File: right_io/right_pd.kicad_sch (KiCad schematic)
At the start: 68 parts, among them J11 USB-C dual-role data/PD port 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, J12 USB-C source-only data port J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, Q2002 2N7002K DFP USB2 enable inver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, U1760 TPS2553DDBVR 1.3A USB branch, U1761 TPS25810RVCR Type-C DFP contr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, U1763 TPD1S514-1YZR 5.9V VBUS OVP, U1765 TPD4E05U06 USB2/CC ESD, U2011 TPD4S201 CC and USB2 short-to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, U2012 CAT24C256 32KB private TPS257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, U2013 TS3USB30E DFP-qualified USB2 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, U2014 SN74LVC2G07 partial-power-dow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, U2015 TVS2200 22V USB VBUS surge cl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, U2016 SN74LVC1G08 DFP and attached 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, U42 TPS25751AD USB-PD DRP control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, U721 TPS26630RGER PD2 default-off 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

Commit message: Phase 5: second-opinion audit remediation + rebuilt, verified board pipeline
Second-opinion AI audit found A-tier defects; remediation applied and the
board pipeline rebuilt on a known-good base with the fixes it needed:

- electrical: LTC4418IUF symbol pinout corrected (both selectors were
  dead as drawn); center charge cascade (U15 <- U15B, PD1 > PD2 > AUX);
  pack negative never crosses FPC-3, 15-pin FG_VSS return; power-budgeted
  FPC pin maps (0.4 A/pin derate); J12/DS4 completed; AUX source fuse
- FH41-68S footprint: 13 datasheet-correct SH pads + SH pin in symbol
- connector geometry settled against the Hirose FH12 2D drawing: FFC
  enters opposite the solder pins (mouth = local +Y); reversed side-B
  maps are correct for the 180-deg-mounted pairs; rotations set so mouths
  face across every seam
- pipeline (generate_split_boards.py): per-pin pad-net resync from the
  netlists (kills shadow nets for good), netlist-exact name
  normalization, netlist-only part injection (cascade, probe headers),
  zone refill after outline swap, read-before-write race fixed, orphan
  parts dropped loudly, non-zero exit on unresolved overlaps
- monolith board relocated to old/monolith_ducktop2.kicad_pcb (placement
  oracle for the center cut only)

verified end state: 4 boards 0 shorts / 0 clearance / 0 drill, 0 boundary
crossings, 6/6 connectors contract-exact with mouths facing, 0 shadow
nets, gates PASS x4, ERC 0 x4. routing next (499 nets/board).
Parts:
- added H13, H15, H17, H27: M2.5 isolated mainboard mounting hole, MountingHole:MountingHole_2.7mm_M2.5, symbol Mechanical:MountingHole
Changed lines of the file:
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@@
 )
 (no_connect (at 388.62 147.32))
-(label "PD2_VBUS_GATED"
+(hierarchical_label "PD2_VBUS_GATED"
+  (shape bidirectional)
   (at 388.62 132.08 0)
   (effects (font (size 1.27 1.27)) (justify left bottom))
 )
-(label "PD2_VBUS_GATED"
+(hierarchical_label "PD2_VBUS_GATED"
+  (shape bidirectional)
   (at 388.62 132.08 0)
   (effects (font (size 1.27 1.27)) (justify left bottom))
@@
   (effects (font (size 1.27 1.27)) (justify left bottom))
 )
-(label "HUB_PRT_CTL4"
+(hierarchical_label "HUB_PRT_CTL4"
+  (shape bidirectional)
   (at 38.1 359.41 0)
   (effects (font (size 1.27 1.27)) (justify left bottom))
 )
-(label "HUB_PRT_CTL4"
+(hierarchical_label "HUB_PRT_CTL4"
+  (shape bidirectional)
   (at 53.34 361.95 0)
   (effects (font (size 1.27 1.27)) (justify left bottom))
@@
   )
 )
-(label "HUB_PRT_CTL4"
+(hierarchical_label "HUB_PRT_CTL4"
+  (shape bidirectional)
   (at 111.76 381 0)
   (effects (font (size 1.27 1.27)) (justify left bottom))
@@
   (effects (font (size 1.27 1.27)) (justify left bottom))
 )
-(label "HUB_PRT_CTL4"
+(hierarchical_label "HUB_PRT_CTL4"
+  (shape bidirectional)
   (at 86.36 375.92 0)
   (effects (font (size 1.27 1.27)) (justify left bottom))
@@
   (effects (font (size 1.27 1.27)) (justify left bottom))
 )
-(label "HUB_DS4_DP"
+(hierarchical_label "HUB_DS4_DP"
+  (shape bidirectional)
   (at 261.62 373.38 0)
   (effects (font (size 1.27 1.27)) (justify left bottom))
 )
-(label "HUB_DS4_DP"
+(hierarchical_label "HUB_DS4_DP"
+  (shape bidirectional)
   (at 261.62 375.92 0)
   (effects (font (size 1.27 1.27)) (justify left bottom))
 )
-(label "HUB_DS4_DM"
+(hierarchical_label "HUB_DS4_DM"
+  (shape bidirectional)
   (at 261.62 368.3 0)
   (effects (font (size 1.27 1.27)) (justify left bottom))
 )
-(label "HUB_DS4_DM"
+(hierarchical_label "HUB_DS4_DM"
+  (shape bidirectional)
   (at 261.62 370.84 0)
   (effects (font (size 1.27 1.27)) (justify left bottom))
@@
 (no_connect (at 271.78 398.78))
 (symbol
+  (lib_id "Mechanical:MountingHole")
+  (at 500.38 20.32 0)
+  (unit 1)
+  (exclude_from_sim no)
+  (in_bom no)
+  (on_board yes)
+  (dnp no)
+  (property "Reference" "H13" (at 500.38 17.78 0) (effects (font (size 1.27 1.27))))
+  (property "Value" "M2.5 isolated mainboard mounting hole" (at 500.38 22.86 0) (effects (font (size 1.27 1.27))))
+  (property "Footprint" "MountingHole:MountingHole_2.7mm_M2.5" (at 500.38 20.32 0) (effects (font (size 1.27 1.27)) (hide yes)))
+  (property "Datasheet" "" (at 500.38 20.32 0) (effects (font (size 1.27 1.27)) (hide yes)))
+  (property "Hardware_Spec" "2.7mm isolated NPTH for M2.5 chassis screw" (at 500.38 20.32 0) (effects (font (size 1.27 1.27)) (hide yes)))
+  (instances
+    (project "ducktop2"
+      (path "/37367af8-d35a-52ce-9a32-1764ce5de36b"
+        (reference "H13")
+        (unit 1)
+      )
+    )
+  )
+)
+(symbol
+  (lib_id "Mechanical:MountingHole")
+  (at 500.38 20.32 0)
+  (unit 1)
+  (exclude_from_sim no)
+  (in_bom no)
+  (on_board yes)
+  (dnp no)
+  (property "Reference" "H15" (at 500.38 17.78 0) (effects (font (size 1.27 1.27))))
+  (property "Value" "M2.5 isolated mainboard mounting hole" (at 500.38 22.86 0) (effects (font (size 1.27 1.27))))
+  (property "Footprint" "MountingHole:MountingHole_2.7mm_M2.5" (at 500.38 20.32 0) (effects (font (size 1.27 1.27)) (hide yes)))
+  (property "Datasheet" "" (at 500.38 20.32 0) (effects (font (size 1.27 1.27)) (hide yes)))
+  (property "Hardware_Spec" "2.7mm isolated NPTH for M2.5 chassis screw" (at 500.38 20.32 0) (effects (font (size 1.27 1.27)) (hide yes)))
+  (instances
+    (project "ducktop2"
+      (path "/37367af8-d35a-52ce-9a32-1764ce5de36b"
+        (reference "H15")
+        (unit 1)
+      )
+    )
+  )
+)
+(symbol
+  (lib_id "Mechanical:MountingHole")
+  (at 500.38 20.32 0)
+  (unit 1)
+  (exclude_from_sim no)
+  (in_bom no)
+  (on_board yes)
+  (dnp no)
+  (property "Reference" "H17" (at 500.38 17.78 0) (effects (font (size 1.27 1.27))))
+  (property "Value" "M2.5 isolated mainboard mounting hole" (at 500.38 22.86 0) (effects (font (size 1.27 1.27))))
+  (property "Footprint" "MountingHole:MountingHole_2.7mm_M2.5" (at 500.38 20.32 0) (effects (font (size 1.27 1.27)) (hide yes)))
+  (property "Datasheet" "" (at 500.38 20.32 0) (effects (font (size 1.27 1.27)) (hide yes)))
+  (property "Hardware_Spec" "2.7mm isolated NPTH for M2.5 chassis screw" (at 500.38 20.32 0) (effects (font (size 1.27 1.27)) (hide yes)))
+  (instances
+    (project "ducktop2"
+      (path "/37367af8-d35a-52ce-9a32-1764ce5de36b"
+        (reference "H17")
+        (unit 1)
+      )
+    )
+  )
+)
+(symbol
+  (lib_id "Mechanical:MountingHole")
+  (at 500.38 20.32 0)
+  (unit 1)
+  (exclude_from_sim no)
+  (in_bom no)
+  (on_board yes)
+  (dnp no)
+  (property "Reference" "H27" (at 500.38 17.78 0) (effects (font (size 1.27 1.27))))
+  (property "Value" "M2.5 isolated mainboard mounting hole" (at 500.38 22.86 0) (effects (font (size 1.27 1.27))))
+  (property "Footprint" "MountingHole:MountingHole_2.7mm_M2.5" (at 500.38 20.32 0) (effects (font (size 1.27 1.27)) (hide yes)))
+  (property "Datasheet" "" (at 500.38 20.32 0) (effects (font (size 1.27 1.27)) (hide yes)))
+  (property "Hardware_Spec" "2.7mm isolated NPTH for M2.5 chassis screw" (at 500.38 20.32 0) (effects (font (size 1.27 1.27)) (hide yes)))
+  (instances
+    (project "ducktop2"
+      (path "/37367af8-d35a-52ce-9a32-1764ce5de36b"
+        (reference "H27")
+        (unit 1)
+      )
+    )
+  )
+)
+(symbol
   (lib_id "power:GND")

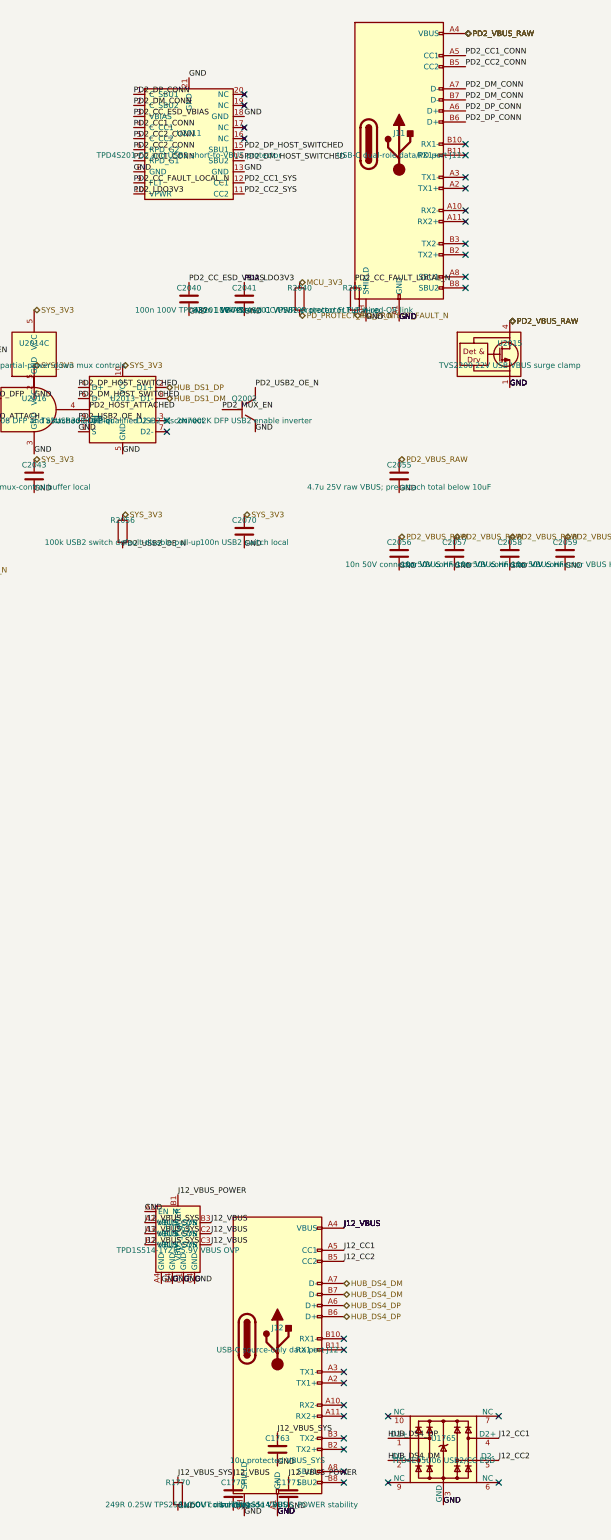
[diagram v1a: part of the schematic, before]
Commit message: get the main boards ready for routing
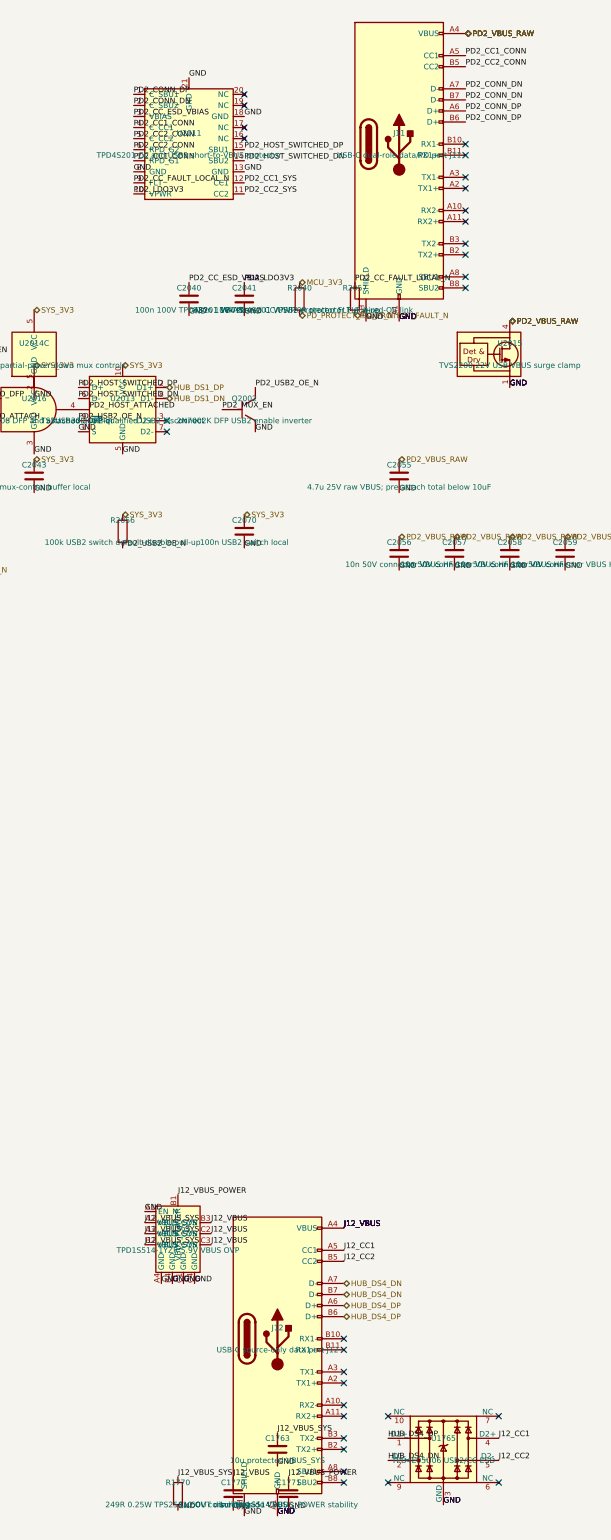
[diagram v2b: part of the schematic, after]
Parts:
- U2011: ChannelUse CC1_CC2_AND_USB2_DP_DM;DEAD_BATTERY_RD_ENABLED -> CC1_CC2_AND_USB2_DP_DN;DEAD_BATTERY_RD_ENABLED
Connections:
- net HUB_DS1_DM renamed HUB_DS1_DN
- net HUB_DS4_DM renamed HUB_DS4_DN
- net PD2_DM_CONN renamed PD2_CONN_DN
- net PD2_DM_HOST_SWITCHED renamed PD2_HOST_SWITCHED_DN
- net PD2_DP_CONN renamed PD2_CONN_DP
- net PD2_DP_HOST_SWITCHED renamed PD2_HOST_SWITCHED_DP
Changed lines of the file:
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@@
   (effects (font (size 1.27 1.27)) (justify left bottom))
 )
-(label "PD2_DP_CONN"
+(label "PD2_CONN_DP"
   (at 289.56 99.06 0)
   (effects (font (size 1.27 1.27)) (justify left bottom))
 )
-(label "PD2_DP_CONN"
+(label "PD2_CONN_DP"
   (at 289.56 101.6 0)
   (effects (font (size 1.27 1.27)) (justify left bottom))
 )
-(label "PD2_DM_CONN"
+(label "PD2_CONN_DN"
   (at 289.56 93.98 0)
   (effects (font (size 1.27 1.27)) (justify left bottom))
 )
-(label "PD2_DM_CONN"
+(label "PD2_CONN_DN"
   (at 289.56 96.52 0)
   (effects (font (size 1.27 1.27)) (justify left bottom))
@@
   (property "MPN" "TPD4S201RUKR" (at 226.06 106.68 0) (effects (font (size 1.27 1.27)) (hide yes)))
   (property "Datasheet" "https://www.ti.com/lit/ds/symlink/tpd4s201.pdf" (at 226.06 106.68 0) (effects (font (size 1.27 1.27)) (hide yes)))
-  (property "ChannelUse" "CC1_CC2_AND_USB2_DP_DM;DEAD_BATTERY_RD_ENABLED" (at 226.06 106.68 0) (effects (font (size 1.27 1.27)) (hide yes)))
+  (property "ChannelUse" "CC1_CC2_AND_USB2_DP_DN;DEAD_BATTERY_RD_ENABLED" (at 226.06 106.68 0) (effects (font (size 1.27 1.27)) (hide yes)))
   (pin "1")
   (pin "2")
@@
   )
 )
-(label "PD2_DP_CONN"
+(label "PD2_CONN_DP"
   (at 213.36 95.25 0)
   (effects (font (size 1.27 1.27)) (justify left bottom))
 )
-(label "PD2_DM_CONN"
+(label "PD2_CONN_DN"
   (at 213.36 97.79 0)
   (effects (font (size 1.27 1.27)) (justify left bottom))
@@
   (effects (font (size 1.27 1.27)) (justify left bottom))
 )
-(label "PD2_DM_HOST_SWITCHED"
+(label "PD2_HOST_SWITCHED_DN"
   (at 238.76 110.49 0)
   (effects (font (size 1.27 1.27)) (justify left bottom))
 )
-(label "PD2_DP_HOST_SWITCHED"
+(label "PD2_HOST_SWITCHED_DP"
   (at 238.76 107.95 0)
   (effects (font (size 1.27 1.27)) (justify left bottom))
@@
 )
 (no_connect (at 220.98 170.18))
-(label "PD2_DP_HOST_SWITCHED"
+(label "PD2_HOST_SWITCHED_DP"
   (at 200.66 162.56 0)
   (effects (font (size 1.27 1.27)) (justify left bottom))
@@
   (effects (font (size 1.27 1.27)) (justify left bottom))
 )
-(label "PD2_DM_HOST_SWITCHED"
+(label "PD2_HOST_SWITCHED_DN"
   (at 200.66 165.1 0)
   (effects (font (size 1.27 1.27)) (justify left bottom))
 )
 (no_connect (at 220.98 172.72))
-(hierarchical_label "HUB_DS1_DM"
+(hierarchical_label "HUB_DS1_DN"
   (shape bidirectional)
   (at 220.98 165.1 0)
@@
   (effects (font (size 1.27 1.27)) (justify left bottom))
 )
-(hierarchical_label "HUB_DS4_DM"
+(hierarchical_label "HUB_DS4_DN"
   (shape bidirectional)
   (at 261.62 368.3 0)
   (effects (font (size 1.27 1.27)) (justify left bottom))
 )
-(hierarchical_label "HUB_DS4_DM"
+(hierarchical_label "HUB_DS4_DN"
   (shape bidirectional)
   (at 261.62 370.84 0)
@@
   (effects (font (size 1.27 1.27)) (justify left bottom))
 )
-(label "HUB_DS4_DM"
+(label "HUB_DS4_DN"
   (at 271.78 408.94 0)
   (effects (font (size 1.27 1.27)) (justify left bottom))

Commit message: fix audit issues and move some connectors
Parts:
- R2090: value 887k 0.1% 15V eFuse UV/OV top -> 8.87k 0.1% 10ppm 15/20V eFuse UV/OV top; MPN RT0603BRD07887KL -> RT0603BRB078K87L
- R2091: value 27.4k 0.1% 15V eFuse UV/OV middle -> 562R 0.1% 10ppm 15/20V eFuse UV/OV middle; MPN RT0603BRD0727K4L -> RT0603BRB07562RL
- R2092: value 68.1k 0.1% 15V eFuse UV/OV bottom -> 511R 0.1% 10ppm 15/20V eFuse UV/OV bottom; MPN RT0603BRD0768K1L -> RT0603BRB07511RL
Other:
- note added: "J11: hardware accepts 15V/20V PD; use a verified 3A contract and 2.50A charger bootstrap limit. EEPROM/profile qualification remains required."
- note removed: "J11: EEPROM configures DRP prefer-sink, 15V/3A sink, 5V/0.9A source, default Rp, GPIO6 FLIP, GPIO4 DFP, and GPIO7 data-attached."

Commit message: fix the center layout and more board issues
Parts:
- removed H27: M2.5 isolated mainboard mounting hole, MountingHole:MountingHole_2.7mm_M2.5, symbol Mechanical:MountingHole
- added C2404: 1u, Capacitor_SMD:C_0805_2012Metric, symbol Device:C
- added C2409: 100n, Capacitor_SMD:C_0603_1608Metric, symbol Device:C
- added C2414: 4.7n C0G PP5V slew, Capacitor_SMD:C_0603_1608Metric, symbol Device:C
- added R2404, R2409: 100k, Resistor_SMD:R_0603_1608Metric, symbol Device:R
- added R2414: 10k, Resistor_SMD:R_0603_1608Metric, symbol Device:R
- added U2404: TPS22992SRXNR J11 PP5V gate, ducktop2:Texas_RXN0008A_WQFN-HR-8_1.25x1.25mm, symbol TPS22992S:TPS22992S
- added U2409: SN74LVC1G08DBVR J12 source permission, Package_TO_SOT_SMD:SOT-23-5, symbol 74xGxx:74LVC1G08
- R1760: value 20.0k 1% TPS2553 1.3A ILIM -> 19.1k 1% TPS2553 VBUS plus VCONN ILIM; MPN RC0603FR-0720KL -> RC0603FR-0719K1L
- R2090: value 8.87k 0.1% 10ppm 15/20V eFuse UV/OV top -> 8.87k 0.02% 5ppm 15/20V eFuse UV/OV top; MPN RT0603BRB078K87L -> TNPU06038K87HZEN00; Manufacturer Yageo -> Vishay
- R2091: value 562R 0.1% 10ppm 15/20V eFuse UV/OV middle -> 562R 0.02% 5ppm 15/20V eFuse UV/OV middle; MPN RT0603BRB07562RL -> TNPU0603562RHZEN00; Manufacturer Yageo -> Vishay
- R2092: value 511R 0.1% 10ppm 15/20V eFuse UV/OV bottom -> 511R 0.02% 5ppm 15/20V eFuse UV/OV bottom; MPN RT0603BRB07511RL -> TNPU0603511RHZEN00; Manufacturer Yageo -> Vishay
- U42: EEPROMSource firmware/tps25751a/ducktop2_dual_role_config.json -> firmware/tps25751a/ducktop2_pd2_config.json; PortPolicy DRP_PREFER_SINK;HOST_DATA_ONLY;15V_3A_SINK;5V_900MA_SOURCE;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 -> DRP;HOST_DATA_ONLY;5_9_15_20V_3A_SINK;5V_900MA_SOURCE;DEFAU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
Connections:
- net GND: now also C2404.2, C2409.2, C2414.2, R2404.2, R2409.2, U2404.4 (GND), U2409.3 (GND)
- net HUB_PRT_CTL4: now also U2409.2; no longer U1760.3 (EN), U1761.6 (EN)
- net MCU_3V3: now also C2409.1, U2409.5 (VCC)
- net USB_PORT_5V: now also C2404.1, U2404.1 (VBIAS), U2404.2 (VIN); no longer C2065.1, C2066.1, C2067.1, U42.34 (PP5V_(34-35))
- new net J11_PP5V_CT: C2414.1, U2404.7 (CT)
- new net PD2_PP5V_GATED: C2065.1, C2066.1, C2067.1, R2414.1, U2404.5 (QOD), U2404.6 (VOUT), U42.34 (PP5V_(34-35))
- new net PD2_SOURCE_PG: R2414.2, U2404.3 (PG)
- new net USB_J11_PERMIT: R2404.1, U2404.8 (ON)
- new net USB_J12_PERMIT: R2409.1, U2409.1
- new net USB_J12_SWITCH_EN: U1760.3 (EN), U1761.6 (EN), U2409.4
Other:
- note added: "J11: hardware accepts 15V/20V PD; use a verified 3A contract and 2.50A IINDPM bootstrap command. Actual current/headroom and EEPROM/profile qualification remain required."
- note removed: "J11: hardware accepts 15V/20V PD; use a verified 3A contract and 2.50A charger bootstrap limit. EEPROM/profile qualification remains required."
